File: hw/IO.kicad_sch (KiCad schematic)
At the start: 11 parts, among them U6 GAQY212GSX

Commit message: Footprints created, starting layout
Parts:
- U6: footprint (none) -> Package_SO:SO-4_4.4x4.3mm_P2.54mm
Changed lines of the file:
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@@
 			)
 		)
-		(property "Footprint" ""
+		(property "Footprint" "Package_SO:SO-4_4.4x4.3mm_P2.54mm"
 			(at 125.73 64.77 0)
 			(effects

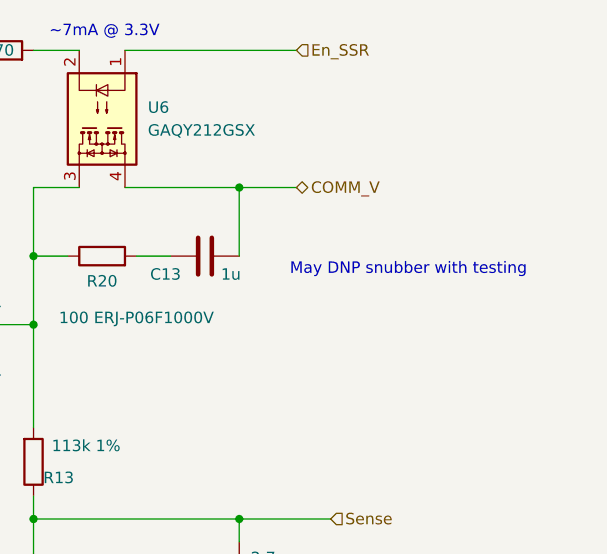
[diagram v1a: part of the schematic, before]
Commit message: Added sense for input voltage and created BOM
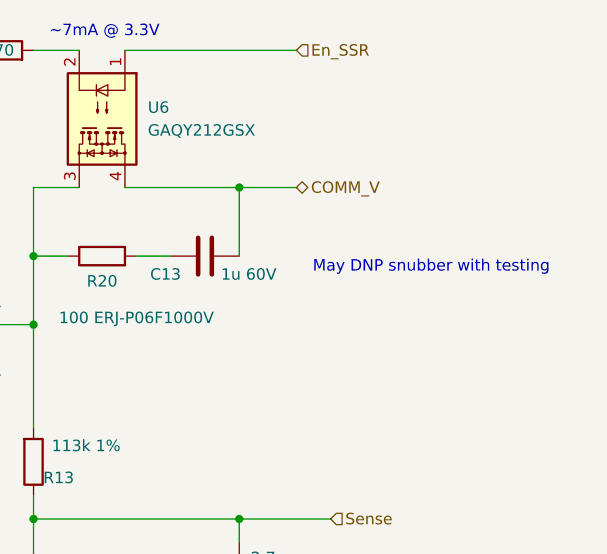
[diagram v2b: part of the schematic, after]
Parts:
- C13: value 1u -> 1u 60V; Manufacturer Part Number (none) -> C1608X7R2A105K080AC
- C14: Manufacturer Part Number (none) -> 0603B272K500CT
- D19, D3: Manufacturer Part Number (none) -> SM4007PL
- D2: Manufacturer Part Number (none) -> SMAJ60CA/TR13
- F2: Manufacturer Part Number (none) -> 0ZCF0075AF2C
- R11: Manufacturer Part Number (none) -> RMCF0603JT270R
- R13: Manufacturer Part Number (none) -> AC0603FR-07113KL
- R18: Manufacturer Part Number (none) -> AC0603FR-075K9L
- R20: Manufacturer Part Number (none) -> ERJ-P06F1000V
- U6: Manufacturer Part Number (none) -> GAQY212GSX
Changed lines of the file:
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@@
 	(text "May DNP snubber with testing"
 		(exclude_from_sim no)
-		(at 164.846 86.614 0)
+		(at 167.386 86.36 0)
 		(effects
 			(font
@@
 			)
 		)
+		(property "Manufacturer Part Number" "0603B272K500CT"
+			(at 146.05 120.65 0)
+			(effects
+				(font
+					(size 1.27 1.27)
+				)
+				(hide yes)
+			)
+		)
 		(pin "1"
 		)
@@
 			)
 		)
+		(property "Manufacturer Part Number" "SM4007PL"
+			(at 107.95 88.9 90)
+			(effects
+				(font
+					(size 1.27 1.27)
+				)
+				(hide yes)
+			)
+		)
 		(pin "1"
 		)
@@
 		(property "Description" "Resistor"
 			(at 130.81 85.09 0)
+			(effects
+				(font
+					(size 1.27 1.27)
+				)
+				(hide yes)
+			)
+		)
+		(property "Manufacturer Part Number" "ERJ-P06F1000V"
+			(at 130.81 85.09 90)
 			(effects
 				(font
@@
 			)
 		)
+		(property "Manufacturer Part Number" "0ZCF0075AF2C"
+			(at 85.09 92.71 90)
+			(effects
+				(font
+					(size 1.27 1.27)
+				)
+				(hide yes)
+			)
+		)
 		(pin "2"
 		)
@@
 			)
 		)
+		(property "Manufacturer Part Number" "GAQY212GSX"
+			(at 130.81 69.85 90)
+			(effects
+				(font
+					(size 1.27 1.27)
+				)
+				(hide yes)
+			)
+		)
 		(pin "1"
 		)
@@
 			)
 		)
-		(property "Value" "1u"
+		(property "Value" "1u 60V"
 			(at 144.018 87.122 90)
 			(effects
@@
 					(size 1.27 1.27)
 				)
+			)
+		)
+		(property "Manufacturer Part Number" "C1608X7R2A105K080AC"
+			(at 142.24 85.09 90)
+			(effects
+				(font
+					(size 1.27 1.27)
+				)
+				(hide yes)
 			)
 		)
@@
 			)
 		)
+		(property "Manufacturer Part Number" "AC0603FR-07113KL"
+			(at 123.19 107.95 0)
+			(effects
+				(font
+					(size 1.27 1.27)
+				)
+				(hide yes)
+			)
+		)
 		(pin "1"
 		)
@@
 			)
 		)
+		(property "Manufacturer Part Number" "SM4007PL"
+			(at 107.95 96.52 90)
+			(effects
+				(font
+					(size 1.27 1.27)
+				)
+				(hide yes)
+			)
+		)
 		(pin "1"
 		)
@@
 			)
 		)
+		(property "Manufacturer Part Number" "SMAJ60CA/TR13"
+			(at 93.98 97.79 90)
+			(effects
+				(font
+					(size 1.27 1.27)
+				)
+				(hide yes)
+			)
+		)
 		(pin "1"
 		)
@@
 			)
 		)
+		(property "Manufacturer Part Number" "RMCF0603JT270R"
+			(at 119.38 62.23 90)
+			(effects
+				(font
+					(size 1.27 1.27)
+				)
+				(hide yes)
+			)
+		)
 		(pin "1"
 		)
@@
 			(at 123.19 121.92 0)
 			(effects
+				(font
+					(size 1.27 1.27)
+				)
+				(hide yes)
+			)
+		)
+		(property "Manufacturer Part Number" "AC0603FR-075K9L"
+			(at 123.19 121.92 0)
+			(effects
